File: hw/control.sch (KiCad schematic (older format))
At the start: 14 parts, among them U202 74HC165, U203 74HC161, U204 74HC574, U205 27C64, U206 27C64, U207 27C64, U208 27C64, U209 74HCT574, U210 74HCT574, U211 74HCT574, U212 74HCT574, U213 74HC00, U214 74HC08

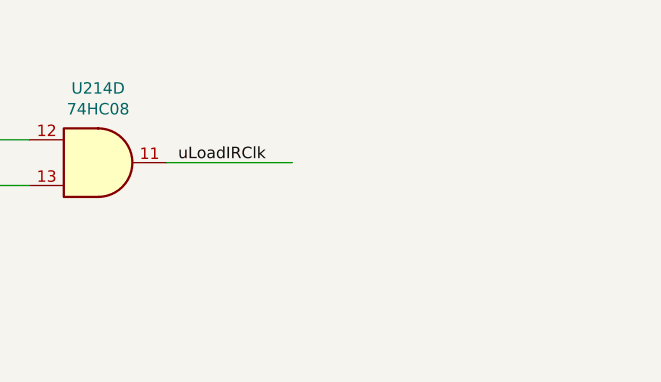
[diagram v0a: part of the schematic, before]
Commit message: some schematic cleanups and descriptive text added
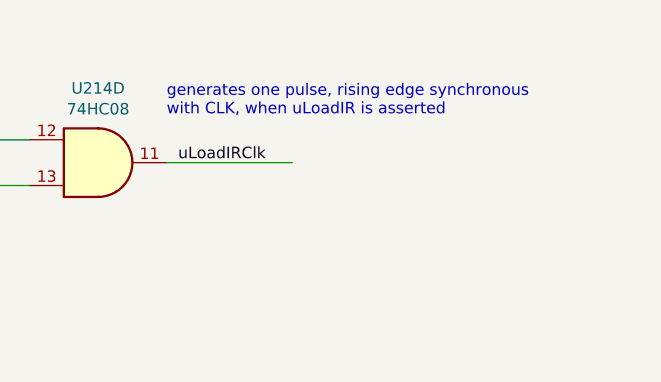
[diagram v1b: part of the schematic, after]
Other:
- note added: "generates one pulse, rising edge synchronous\nwith CLK, when uLoadIR is asserted"
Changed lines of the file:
@@
 Wire Bus Line
 	6350 700  6350 9050
+Text Notes 12600 950  0    50   ~ 0
+generates one pulse, rising edge synchronous\nwith CLK, when uLoadIR is asserted
 $EndSCHEMATC

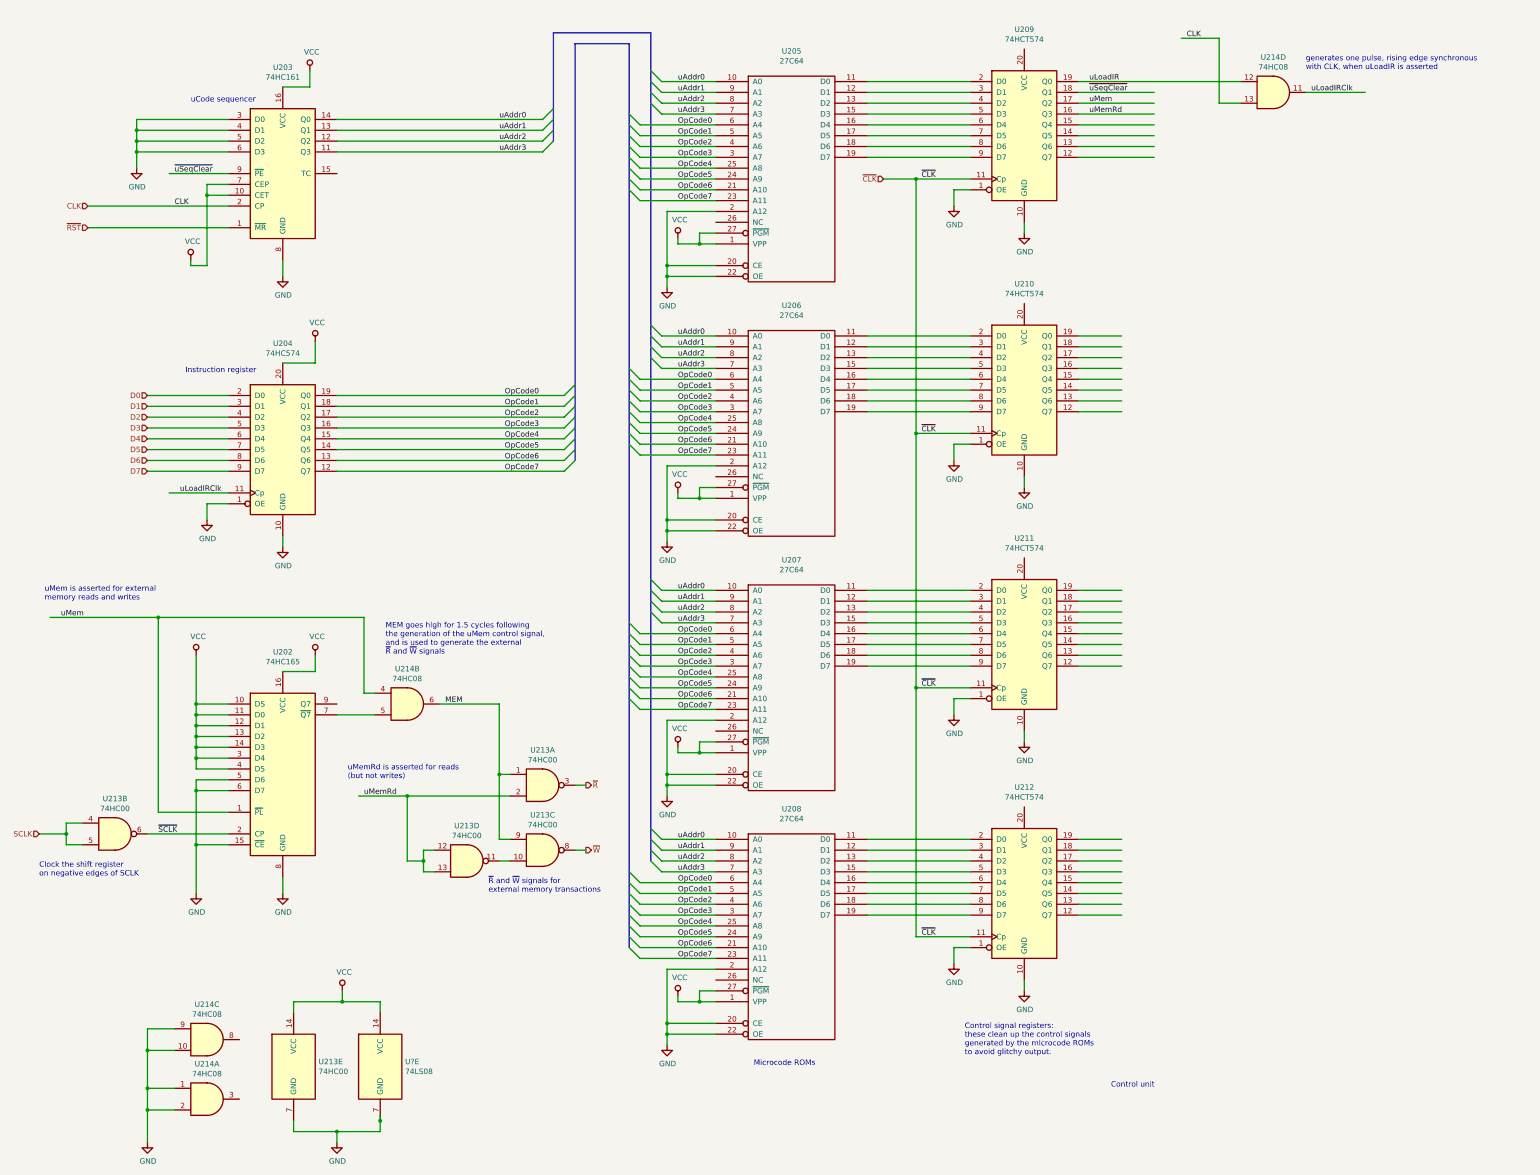
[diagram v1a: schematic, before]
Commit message: use '273 registers for ucode, initial PC design
The microcode registers need to be reset to a known
state on startup.  The 74HCT273 is appropriate for this.
One consequence is that all microcode signals must be
designed such that a 0 is the correct output for
coming out of reset: the main thing that needs to
happen is putting an initial value into the program
counter.  I'm assuming that a '541 buffer will
put an appropriate byte value (maybe 0xC0) on the
D bus on reset, and the PC can load this in both
bytes (so, effective initial PC of 0xC0C0).

Created an initial design for the program counter.
Used 74HC191 synchronous counters, with a 74HC10
triple 3-input NAND to enable counting for each 4
bits as appopriate based on the terminal count status
of the prior counters.
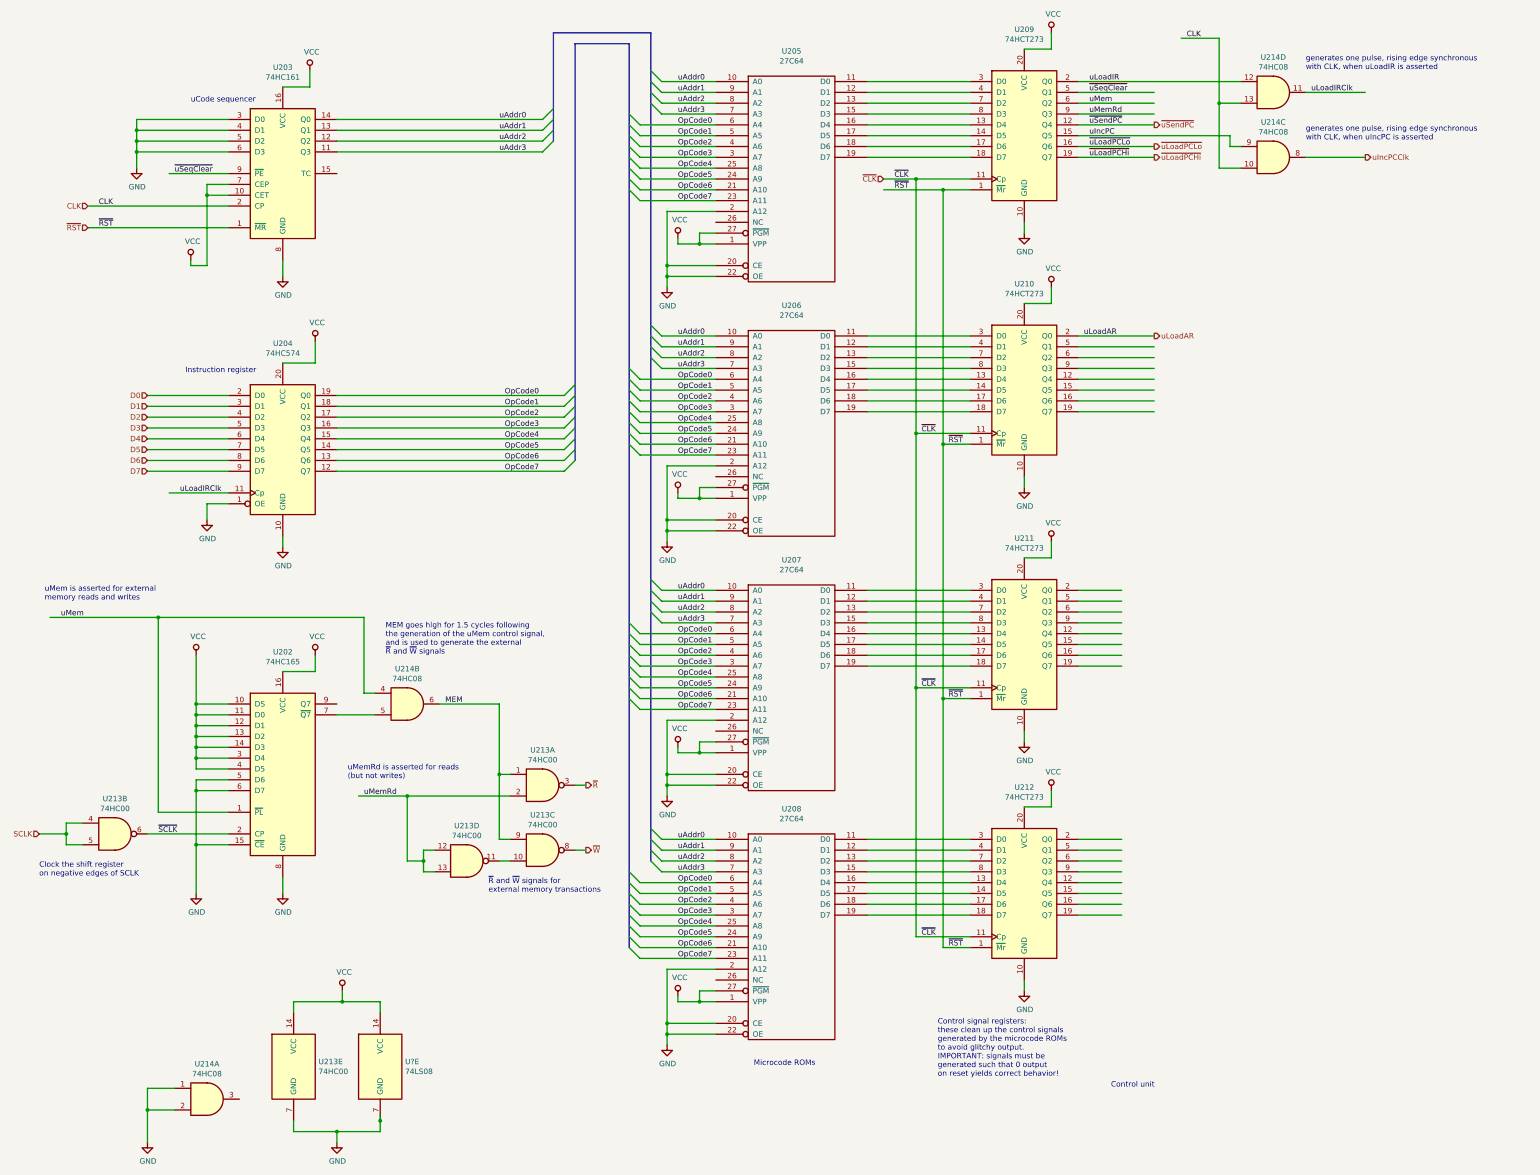
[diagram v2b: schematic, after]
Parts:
- removed U209, U210, U211, U212: 74HCT574, symbol 74xx:74LS574
- added U209, U210, U211, U212: 74HCT273, symbol 74xx:74LS273
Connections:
- net labels added: uIncPC, uIncPCClk, uLoadAR, ~uLoadPCHi, ~uLoadPCLo, ~uSendPC
- wire segments 297 -> 306
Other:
- note added: "Control signal registers:\nthese clean up the control signals\ngenerated by the microcode ROMs\nto avoid glitchy output.\nIMPORTANT: signals must be\ngenerated such that 0 output\non reset yields correct behavior!"
- note added: "generates one pulse, rising edge synchronous\nwith CLK, when uIncPC is asserted"
- note removed: "Control signal registers:\nthese clean up the control signals\ngenerated by the microcode ROMs\nto avoid glitchy output."
- moved on the sheet: U214C
